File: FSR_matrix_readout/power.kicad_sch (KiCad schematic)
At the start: 7 parts, among them U25 TPS7A2033PDBVR, U26 LM321

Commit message: fix Vg-related issuies
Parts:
- added C76: 1uF, symbol Device:C_Small
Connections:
- net GND: now also C76.1
- net V_{g}: now also C76.2
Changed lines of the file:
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@@
+	)
+	(junction
+		(at 162.56 77.47)
+		(diameter 0)
+		(color 0 0 0 0)
 	)
 	(junction
@@
 	(wire
 		(pts
+			(xy 162.56 77.47) (xy 167.64 77.47)
+		)
+		(stroke
+			(width 0)
+			(type default)
+		)
+	)
+	(wire
+		(pts
 			(xy 69.85 63.5) (xy 72.39 63.5)
 		)
@@
 	(wire
 		(pts
-			(xy 152.4 77.47) (xy 157.48 77.47)
+			(xy 152.4 77.47) (xy 162.56 77.47)
 		)
 		(stroke
@@
 	(hierarchical_label "V_{g}"
 		(shape output)
-		(at 157.48 77.47 0)
+		(at 167.64 77.47 0)
 		(effects
 			(font
@@
 	)
 	(symbol
+		(lib_id "Device:C_Small")
+		(at 162.56 80.01 180)
+		(unit 1)
+		(body_style 1)
+		(exclude_from_sim no)
+		(in_bom yes)
+		(on_board yes)
+		(in_pos_files yes)
+		(dnp no)
+		(property "Reference" "C76"
+			(at 156.464 79.502 0)
+			(show_name no)
+			(do_not_autoplace no)
+			(effects
+				(font
+					(size 1.27 1.27)
+				)
+				(justify right)
+			)
+		)
+		(property "Value" "1uF"
+			(at 156.718 81.28 0)
+			(show_name no)
+			(do_not_autoplace no)
+			(effects
+				(font
+					(size 1.27 1.27)
+				)
+				(justify right)
+			)
+		)
+		(property "Footprint" ""
+			(at 162.56 80.01 0)
+			(hide yes)
+			(show_name no)
+			(do_not_autoplace no)
+			(effects
+				(font
+					(size 1.27 1.27)
+				)
+			)
+		)
+		(property "Datasheet" ""
+			(at 162.56 80.01 0)
+			(hide yes)
+			(show_name no)
+			(do_not_autoplace no)
+			(effects
+				(font
+					(size 1.27 1.27)
+				)
+			)
+		)
+		(property "Description" "Unpolarized capacitor, small symbol"
+			(at 162.56 80.01 0)
+			(hide yes)
+			(show_name no)
+			(do_not_autoplace no)
+			(effects
+				(font
+					(size 1.27 1.27)
+				)
+			)
+		)
+		(pin "1"
+		)
+		(pin "2"
+		)
+		(instances
+			(project "FSR_matrix_readout"
+				(path "/6dca5e5c-f676-465d-98c9-14af6047a226/8a1936ee-bbc8-45c2-b1d1-45af2be9c99e"
+					(reference "C76")
+					(unit 1)
+				)
+			)
+		)
+	)
+	(symbol
 		(lib_id "power:GND")
 		(at 120.65 81.28 0)
@@
 					(unit 1)
 				)
+			)
+		)
+	)
+	(symbol
+		(lib_id "power:GND")
+		(at 162.56 82.55 0)
+		(unit 1)
+		(body_style 1)
+		(exclude_from_sim no)
+		(in_bom yes)
+		(on_board yes)
+		(in_pos_files yes)
+		(dnp no)
+		(fields_autoplaced yes)
+		(property "Reference" "#PWR0152"
+			(at 162.56 88.9 0)
+			(hide yes)
+			(show_name no)
+			(do_not_autoplace no)
+			(effects
+				(font
+					(size 1.27 1.27)
+				)
+			)
+		)
+		(property "Value" "GND"
+			(at 162.56 87.63 0)
+			(show_name no)
+			(do_not_autoplace no)
+			(effects
+				(font
+					(size 1.27 1.27)
+				)
+			)
+		)
+		(property "Footprint" ""
+			(at 162.56 82.55 0)
+			(hide yes)
+			(show_name no)
+			(do_not_autoplace no)
+			(effects
+				(font
+					(size 1.27 1.27)
+				)
+			)
+		)
+		(property "Datasheet" ""
+			(at 162.56 82.55 0)
+			(hide yes)
+			(show_name no)
+			(do_not_autoplace no)
+			(effects
+				(font
+					(size 1.27 1.27)
+				)
+			)
+		)
+		(property "Description" "Power symbol creates a global label with name \"GND\" , ground"
+			(at 162.56 82.55 0)
+			(hide yes)
+			(show_name no)
+			(do_not_autoplace no)
+			(effects
+				(font
+					(size 1.27 1.27)
+				)
+			)
+		)
+		(pin "1"
+		)
+		(instances
+			(project "FSR_matrix_readout"
+				(path "/6dca5e5c-f676-465d-98c9-14af6047a226/8a1936ee-bbc8-45c2-b1d1-45af2be9c99e"
+					(reference "#PWR0152")
+					(unit 1)
+				)

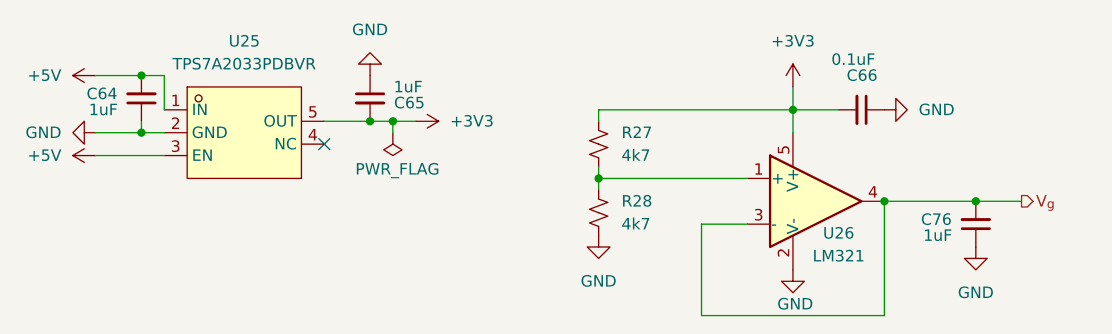
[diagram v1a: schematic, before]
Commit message: add esp devboard module and finished connection
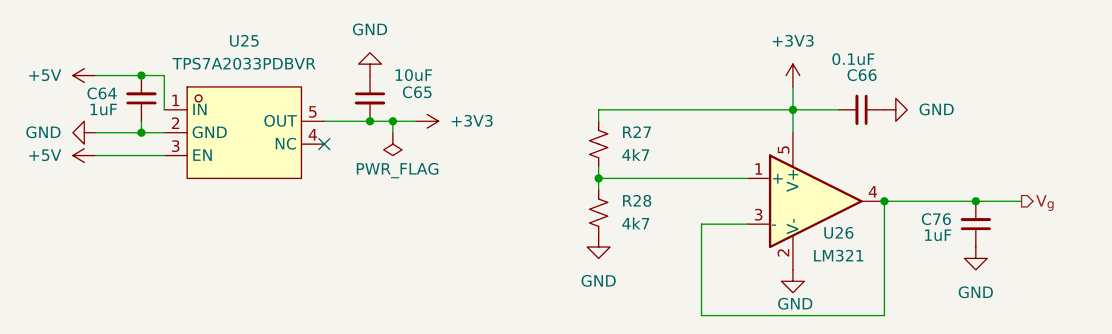
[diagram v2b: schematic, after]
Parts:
- C65: value 1uF -> 10uF
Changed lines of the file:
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@@
 		(instances
 			(project "FSR_matrix_readout"
-				(path "/6dca5e5c-f676-465d-98c9-14af6047a226"
-					(reference "U26")
-					(unit 1)
-				)
 				(path "/6dca5e5c-f676-465d-98c9-14af6047a226/8a1936ee-bbc8-45c2-b1d1-45af2be9c99e"
 					(reference "U26")
@@
 		(instances
 			(project "FSR_matrix_readout"
-				(path "/6dca5e5c-f676-465d-98c9-14af6047a226"
-					(reference "C64")
-					(unit 1)
-				)
 				(path "/6dca5e5c-f676-465d-98c9-14af6047a226/8a1936ee-bbc8-45c2-b1d1-45af2be9c99e"
 					(reference "C64")
@@
 		(instances
 			(project "FSR_matrix_readout"
-				(path "/6dca5e5c-f676-465d-98c9-14af6047a226"
-					(reference "U25")
-					(unit 1)
-				)
 				(path "/6dca5e5c-f676-465d-98c9-14af6047a226/8a1936ee-bbc8-45c2-b1d1-45af2be9c99e"
 					(reference "U25")
@@
 		(instances
 			(project "FSR_matrix_readout"
-				(path "/6dca5e5c-f676-465d-98c9-14af6047a226"
-					(reference "R27")
-					(unit 1)
-				)
 				(path "/6dca5e5c-f676-465d-98c9-14af6047a226/8a1936ee-bbc8-45c2-b1d1-45af2be9c99e"
 					(reference "R27")
@@
 		(dnp no)
 		(property "Reference" "C65"
-			(at 101.346 66.548 0)
+			(at 102.235 65.405 0)
 			(show_name no)
 			(do_not_autoplace no)
@@
 			)
 		)
-		(property "Value" "1uF"
-			(at 101.092 64.77 0)
+		(property "Value" "10uF"
+			(at 102.235 63.5 0)
 			(show_name no)
 			(do_not_autoplace no)
@@
 		(instances
 			(project "FSR_matrix_readout"
-				(path "/6dca5e5c-f676-465d-98c9-14af6047a226"
-					(reference "#FLG01")
-					(unit 1)
-				)
 				(path "/6dca5e5c-f676-465d-98c9-14af6047a226/8a1936ee-bbc8-45c2-b1d1-45af2be9c99e"
 					(reference "#FLG01")
@@
 		(instances
 			(project "FSR_matrix_readout"
-				(path "/6dca5e5c-f676-465d-98c9-14af6047a226"
-					(reference "#PWR0129")
-					(unit 1)
-				)
 				(path "/6dca5e5c-f676-465d-98c9-14af6047a226/8a1936ee-bbc8-45c2-b1d1-45af2be9c99e"
 					(reference "#PWR0129")
@@
 		(instances
 			(project "FSR_matrix_readout"
-				(path "/6dca5e5c-f676-465d-98c9-14af6047a226"
-					(reference "#PWR0127")
-					(unit 1)
-				)
 				(path "/6dca5e5c-f676-465d-98c9-14af6047a226/8a1936ee-bbc8-45c2-b1d1-45af2be9c99e"
 					(reference "#PWR0127")
@@
 		(instances
 			(project "FSR_matrix_readout"
-				(path "/6dca5e5c-f676-465d-98c9-14af6047a226"
+				(path "/6dca5e5c-f676-465d-98c9-14af6047a226/8a1936ee-bbc8-45c2-b1d1-45af2be9c99e"
 					(reference "#PWR0126")
-					(unit 1)
-				)
-				(path "/6dca5e5c-f676-465d-98c9-14af6047a226/8a1936ee-bbc8-45c2-b1d1-45af2be9c99e"
-					(reference "#PWR0126")
